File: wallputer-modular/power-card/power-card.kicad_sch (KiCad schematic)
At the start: 134 parts, among them J2 Power, Q1 FQP27P06, Q2 IRLZ44N, SW1 reset, U1 TLC555CD, U12 74HC04, U16 74HC04, U17 74HC04, U18 74HC04, U2 74HC04, U3 74HC04

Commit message: begin wiring memory card
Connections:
- net NC30 renamed ROM_PGM/
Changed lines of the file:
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@@
 		)
 	)
-	(global_label "NC30"
+	(global_label "ROM_PGM{slash}"
 		(shape input)
 		(at 36.83 171.45 0)
@@
 		)
 	)
-	(global_label "NC30"
+	(global_label "ROM_PGM{slash}"
 		(shape input)
 		(at 213.36 101.6 270)

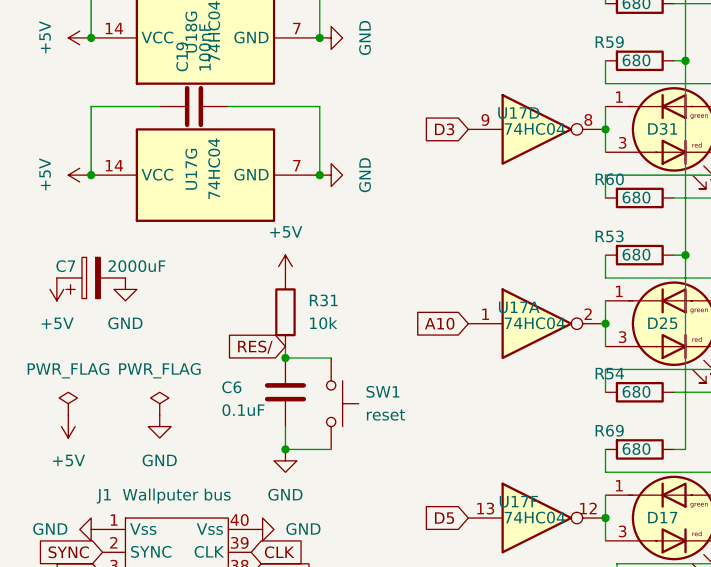
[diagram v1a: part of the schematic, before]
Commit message: do cpu card layout; add git hook; fix project settings
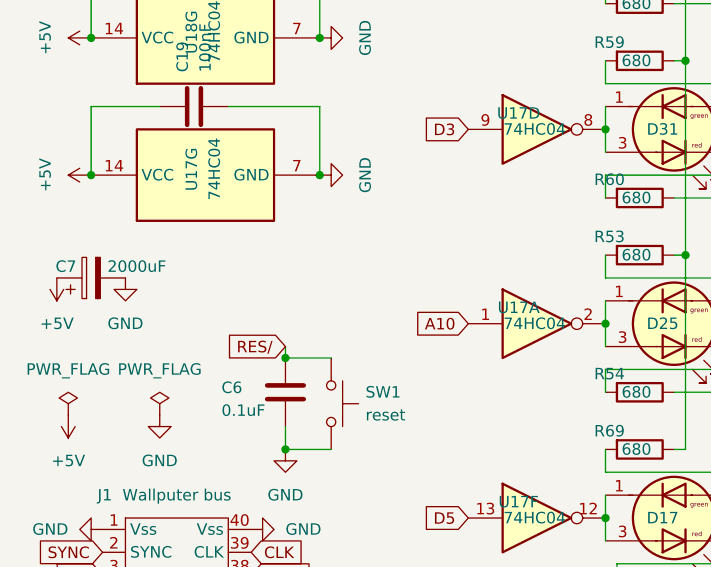
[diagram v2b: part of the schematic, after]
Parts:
- removed R31: 10k, Resistor_THT:R_Axial_DIN0204_L3.6mm_D1.6mm_P2.54mm_Vertical, symbol Device:R
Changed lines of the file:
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@@
 	)
 	(symbol
-		(lib_id "power:+5V")
-		(at 40.64 118.11 0)
-		(unit 1)
-		(exclude_from_sim no)
-		(in_bom yes)
-		(on_board yes)
-		(dnp no)
-		(fields_autoplaced yes)
-		(property "Reference" "#PWR019"
-			(at 40.64 121.92 0)
-			(effects
-				(font
-					(size 1.27 1.27)
-				)
-				(hide yes)
-			)
-		)
-		(property "Value" "+5V"
-			(at 40.64 113.03 0)
-			(effects
-				(font
-					(size 1.27 1.27)
-				)
-			)
-		)
-		(property "Footprint" ""
-			(at 40.64 118.11 0)
-			(effects
-				(font
-					(size 1.27 1.27)
-				)
-				(hide yes)
-			)
-		)
-		(property "Datasheet" ""
-			(at 40.64 118.11 0)
-			(effects
-				(font
-					(size 1.27 1.27)
-				)
-				(hide yes)
-			)
-		)
-		(property "Description" "Power symbol creates a global label with name \"+5V\""
-			(at 40.64 118.11 0)
-			(effects
-				(font
-					(size 1.27 1.27)
-				)
-				(hide yes)
-			)
-		)
-		(pin "1"
-		)
-		(instances
-			(project "power-card"
-				(path "/27eadfe8-fd7c-478e-bb9f-863e2465d9f9"
-					(reference "#PWR019")
-					(unit 1)
-				)
-			)
-		)
-	)
-	(symbol
 		(lib_id "Device:R")
 		(at 80.01 30.48 270)
@@
 					(unit 1)
 				)
-			)
-		)
-	)
-	(symbol
-		(lib_id "Device:R")
-		(at 40.64 121.92 0)
-		(unit 1)
-		(exclude_from_sim no)
-		(in_bom yes)
-		(on_board yes)
-		(dnp no)
-		(fields_autoplaced yes)
-		(property "Reference" "R31"
-			(at 43.18 120.6499 0)
-			(effects
-				(font
-					(size 1.27 1.27)
-				)
-				(justify left)
-			)
-		)
-		(property "Value" "10k"
-			(at 43.18 123.1899 0)
-			(effects
-				(font
-					(size 1.27 1.27)
-				)
-				(justify left)
-			)
-		)
-		(property "Footprint" "Resistor_THT:R_Axial_DIN0204_L3.6mm_D1.6mm_P2.54mm_Vertical"
-			(at 38.862 121.92 90)
-			(effects
-				(font
-					(size 1.27 1.27)
-				)
-				(hide yes)
-			)
-		)
-		(property "Datasheet" "~"
-			(at 40.64 121.92 0)
-			(effects
-				(font
-					(size 1.27 1.27)
-				)
-				(hide yes)
-			)
-		)
-		(property "Description" "Resistor"
-			(at 40.64 121.92 0)
-			(effects
-				(font
-					(size 1.27 1.27)
-				)
-				(hide yes)
-			)
-		)
-		(pin "2"
-		)
-		(pin "1"
-		)
-		(instances
-			(project ""
-				(path "/27eadfe8-fd7c-478e-bb9f-863e2465d9f9"
-					(reference "R31")
-					(unit 1)
-				)
